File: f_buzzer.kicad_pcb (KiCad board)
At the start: 2 copper layers, 71.5 x 44 mm, 10 parts, among them U1 SN74123N

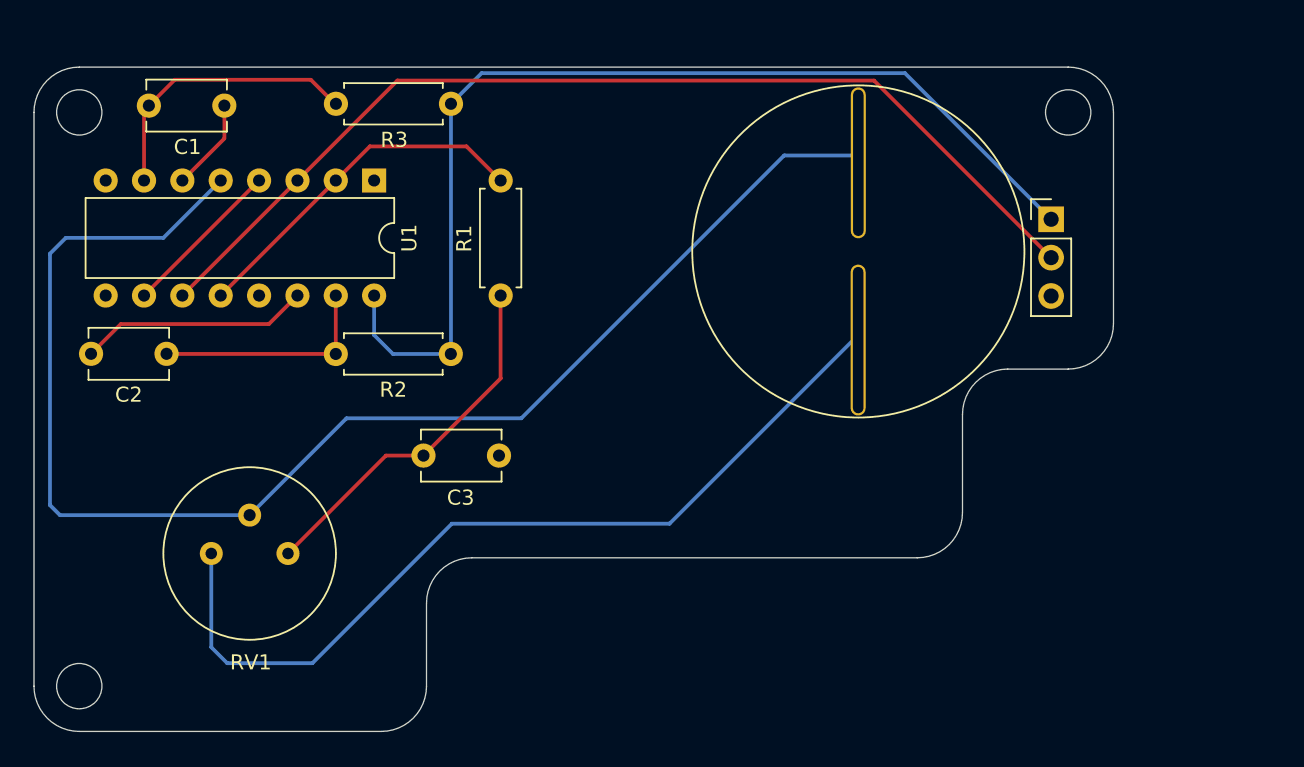
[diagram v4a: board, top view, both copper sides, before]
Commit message: Placed the two buzzers for 3D rendering of the board
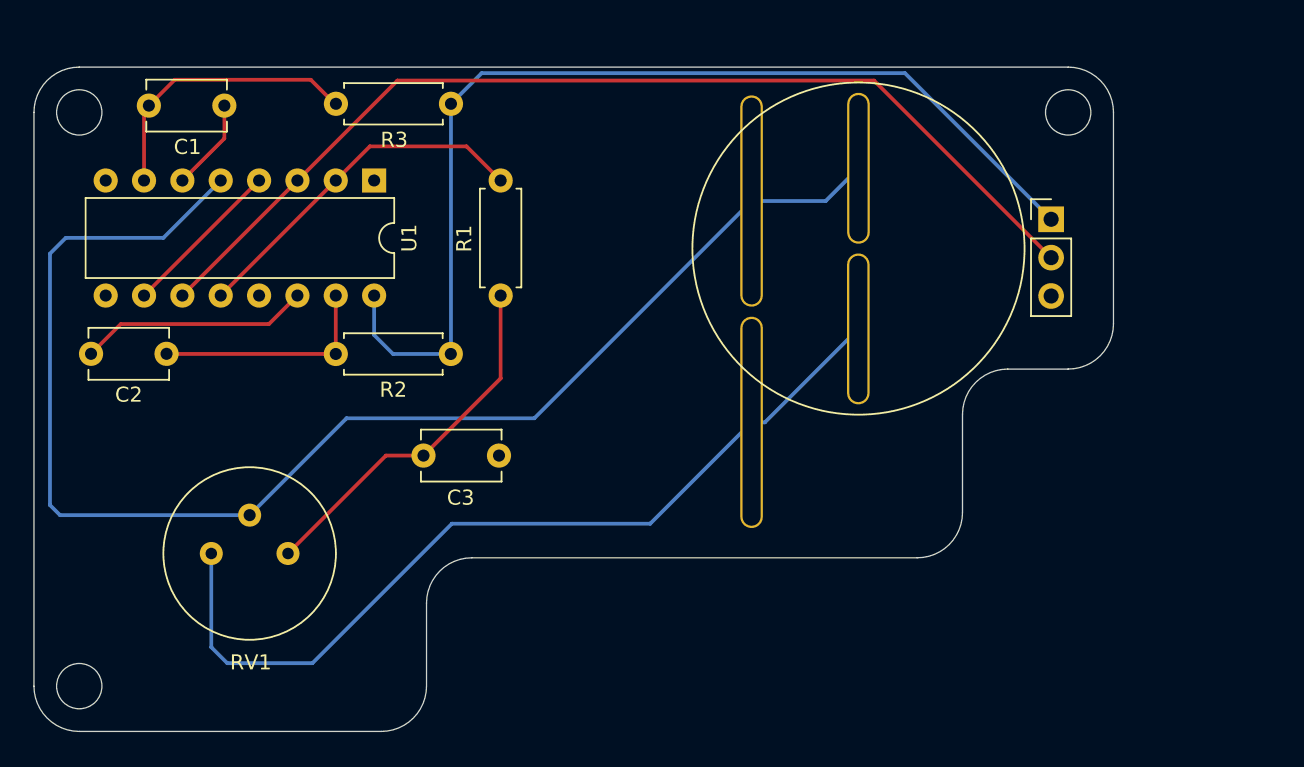
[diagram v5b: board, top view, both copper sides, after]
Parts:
- added BZ1: Buzzer, f_buzzer:buzzer_bottom, B.Cu at (161.7, 92.3)
- moved BZ2 0.19 mm to (168.8, 88.2)
- renumbered BZ1 to BZ2
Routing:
- net Net-(BZ1-Pad1): track 93.8 -> 93.3 mm
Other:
- board text removed: "This is the area where the buzzer could fit on the top of the board."
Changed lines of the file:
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@@
   (general
     (thickness 1.6)
-    (drawings 48)
-    (tracks 51)
+    (drawings 44)
+    (tracks 54)
     (zones 0)
-    (modules 10)
+    (modules 11)
     (nets 14)
   )
@@
     (36 B.SilkS user)
     (37 F.SilkS user)
-    (38 B.Mask user)
-    (39 F.Mask user)
-    (40 Dwgs.User user)
-    (41 Cmts.User user)
+    (38 B.Mask user hide)
+    (39 F.Mask user hide)
+    (40 Dwgs.User user hide)
+    (41 Cmts.User user hide)
     (42 Eco1.User user hide)
     (43 Eco2.User user hide)
@@
     (47 F.CrtYd user hide)
     (48 B.Fab user hide)
-    (49 F.Fab user)
+    (49 F.Fab user hide)
   )
   (setup
@@
     (add_net VCC)
   )
+  (module f_buzzer:buzzer_bottom (layer B.Cu)
+    (at 161.74 92.35 180)
+    (fp_text reference BZ1 (at -0.02 15.2) (layer B.SilkS) hide
+      (effects (font (size 1 1) (thickness 0.15)) (justify mirror))
+    )
+    (fp_text value Buzzer (at -0.09 -15.54) (layer B.Fab)
+      (effects (font (size 1 1) (thickness 0.15)) (justify mirror))
+    )
+    (fp_circle (center 0 0) (end 14.884743 0) (layer B.Fab) (width 0.12))
+    (fp_circle (center 0 0) (end 15 0) (layer B.SilkS) (width 0.12))
+    (pad 2 thru_hole oval (at 0 -7.33 180) (size 1.5 14) (drill oval 1.2 13.7) (layers *.Cu *.Mask)
+      (net 1 "Net-(BZ1-Pad2)"))
+    (pad 1 thru_hole oval (at 0 7.33 180) (size 1.5 14) (drill oval 1.2 13.7) (layers *.Cu *.Mask)
+      (net 2 "Net-(BZ1-Pad1)"))
+    (model f_buzzer.pretty/CUI_DEVICES_CPT-3075-90T.step
+      (offset (xyz 0 0 7.5))
+      (scale (xyz 1 1 1))
+      (rotate (xyz -90 0 -90))
+    )
+  )
   (module f_buzzer:buzzer_front (layer F.Cu)
-    (at 168.81 88.36)
-    (fp_text reference BZ1 (at -0.02 -12.32) (layer F.SilkS) hide
+    (at 168.82 88.17)
+    (fp_text reference BZ2 (at -0.02 -12.32) (layer F.SilkS) hide
       (effects (font (size 1 1) (thickness 0.15)))
     )
@@
       (effects (font (size 1 1) (thickness 0.15)))
     )
-    (fp_circle (center 0 0) (end 8.59 6.68) (layer F.Fab) (width 0.12))
+    (fp_circle (center 0 0) (end 10.881659 0) (layer F.Fab) (width 0.12))
     (fp_circle (center 0 0) (end 11 0) (layer F.SilkS) (width 0.12))
-    (pad 1 thru_hole oval (at 0 -5.87) (size 1 10) (drill oval 0.7 9.7) (layers *.Cu *.Mask)
+    (pad 2 thru_hole oval (at -0.01 5.32) (size 1.5 10) (drill oval 1.2 9.7) (layers *.Cu *.Mask)
+      (net 1 "Net-(BZ1-Pad2)"))
+    (pad 1 thru_hole oval (at 0 -5.32) (size 1.5 10) (drill oval 1.2 9.7) (layers *.Cu *.Mask)
       (net 2 "Net-(BZ1-Pad1)"))
-    (pad 2 thru_hole oval (at -0.01 5.87) (size 1 10) (drill oval 0.7 9.7) (layers *.Cu *.Mask)
-      (net 1 "Net-(BZ1-Pad2)"))
+    (model f_buzzer.pretty/CUI_DEVICES_CPT-2207-84T.step
+      (offset (xyz 0 0 7.5))
+      (scale (xyz 1 1 1))
+      (rotate (xyz -90 0 90))
+    )
   )
   (module Package_DIP:DIP-16_W7.62mm (layer F.Cu)
@@
   (gr_line (start 118.75 76.15) (end 118.75 82) (layer Dwgs.User) (width 0.12))
   (gr_circle (center 179.05 79.2) (end 181.05 79.2) (layer Dwgs.User) (width 0.12))
-  (gr_text "This is the area where the buzzer could fit on the top of the board." (at 207.06 110.52) (layer Cmts.User)
-    (effects (font (size 1 1) (thickness 0.15)))
-  )
-  (gr_line (start 177.82 95.34) (end 178.34 95.37) (layer Cmts.User) (width 0.12))
-  (gr_line (start 177.82 95.34) (end 177.92 95.84) (layer Cmts.User) (width 0.12))
-  (gr_line (start 177.82 95.35) (end 191.65 109.08) (layer Cmts.User) (width 0.12))
   (gr_text "No components should be placed inside the cercle.\nThis where the IBM 4704 series keyboard feet attaches to the back case." (at 120.87 125.39) (layer Cmts.User)
     (effects (font (size 1 1) (thickness 0.15)))
@@
   (gr_line (start 182.71 76.15) (end 117.21 76.15) (layer Edge.Cuts) (width 0.05))
   (gr_line (start 114.21 117.15) (end 114.21 79.15) (layer Edge.Cuts) (width 0.05))
+  (segment (start 125.955 114.575) (end 125.955 108.365) (width 0.25) (layer B.Cu) (net 1))
+  (segment (start 132.65 115.63) (end 127.01 115.63) (width 0.25) (layer B.Cu) (net 1))
+  (segment (start 141.89 106.39) (end 132.65 115.63) (width 0.25) (layer B.Cu) (net 1))
+  (segment (start 155.03 106.39) (end 141.89 106.39) (width 0.25) (layer B.Cu) (net 1))
   (segment (start 127.01 115.63) (end 125.955 114.575) (width 0.25) (layer B.Cu) (net 1))
-  (segment (start 132.65 115.63) (end 127.01 115.63) (width 0.25) (layer B.Cu) (net 1))
-  (segment (start 125.955 114.575) (end 125.955 108.365) (width 0.25) (layer B.Cu) (net 1))
-  (segment (start 156.31 106.39) (end 141.89 106.39) (width 0.25) (layer B.Cu) (net 1))
-  (segment (start 141.89 106.39) (end 132.65 115.63) (width 0.25) (layer B.Cu) (net 1))
-  (segment (start 168.96 93.74) (end 156.31 106.39) (width 0.25) (layer B.Cu) (net 1))
+  (segment (start 161.74 99.68) (end 155.03 106.39) (width 0.25) (layer B.Cu) (net 1))
+  (segment (start 162.62 99.68) (end 168.81 93.49) (width 0.25) (layer B.Cu) (net 1))
+  (segment (start 161.74 99.68) (end 162.62 99.68) (width 0.25) (layer B.Cu) (net 1))
   (segment (start 116.32 87.46) (end 122.78 87.46) (width 0.25) (layer B.Cu) (net 2))
   (segment (start 115.27 88.51) (end 116.32 87.46) (width 0.25) (layer B.Cu) (net 2))
@@
   (segment (start 115.935 105.825) (end 115.27 105.16) (width 0.25) (layer B.Cu) (net 2))
   (segment (start 128.495 105.825) (end 115.935 105.825) (width 0.25) (layer B.Cu) (net 2))
+  (segment (start 147.35 99.41) (end 134.91 99.41) (width 0.25) (layer B.Cu) (net 2))
   (segment (start 134.91 99.41) (end 128.495 105.825) (width 0.25) (layer B.Cu) (net 2))
-  (segment (start 146.49 99.41) (end 134.91 99.41) (width 0.25) (layer B.Cu) (net 2))
-  (segment (start 163.9 82) (end 146.49 99.41) (width 0.25) (layer B.Cu) (net 2))
-  (segment (start 168.97 82) (end 163.9 82) (width 0.25) (layer B.Cu) (net 2))
+  (segment (start 161.74 85.02) (end 147.35 99.41) (width 0.25) (layer B.Cu) (net 2))
+  (segment (start 166.65 85.02) (end 168.82 82.85) (width 0.25) (layer B.Cu) (net 2))
+  (segment (start 161.74 85.02) (end 166.65 85.02) (width 0.25) (layer B.Cu) (net 2))
   (segment (start 121.5 79.02) (end 121.5 83.66) (width 0.25) (layer F.Cu) (net 3))
   (segment (start 121.82 78.7) (end 121.5 79.02) (width 0.25) (layer F.Cu) (net 3))

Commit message: Added fill zones
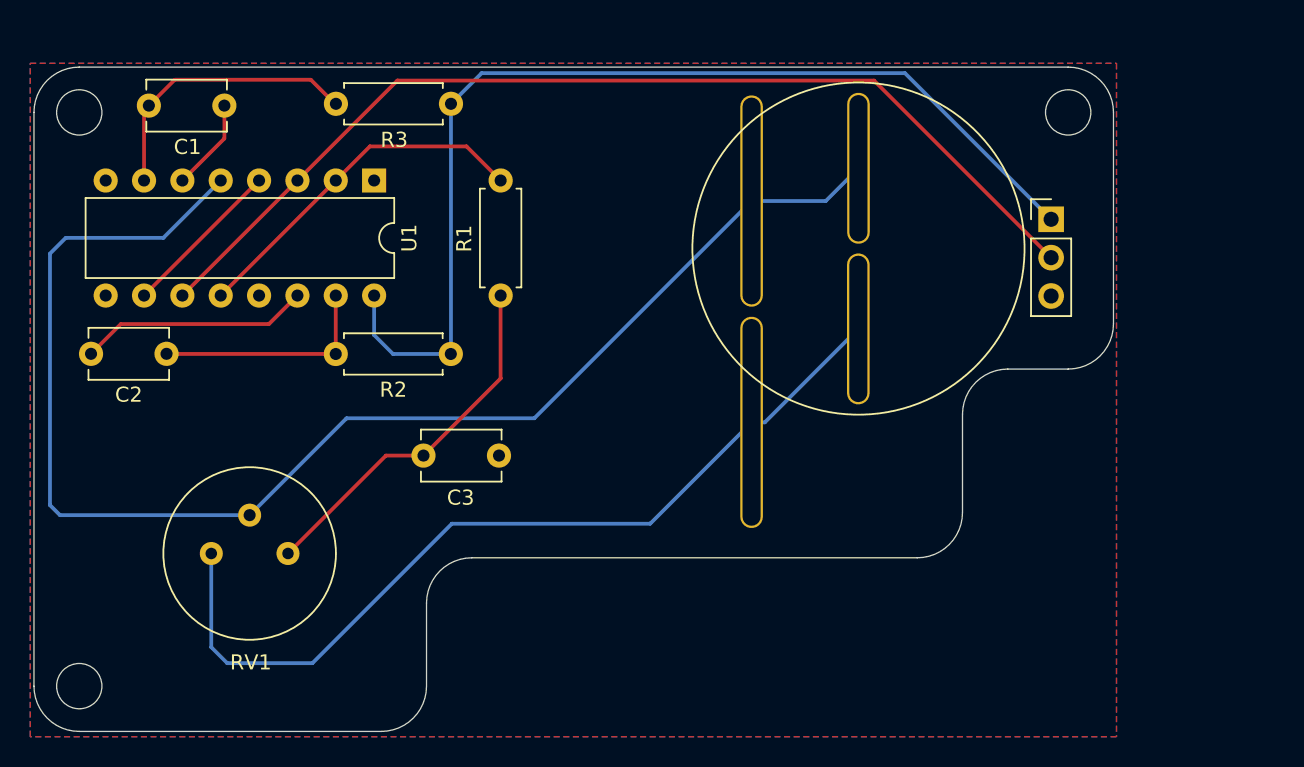
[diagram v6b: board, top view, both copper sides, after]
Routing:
- added copper zone on B.Cu, net GND
- added copper zone on F.Cu, net GND

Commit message: Relocated some components
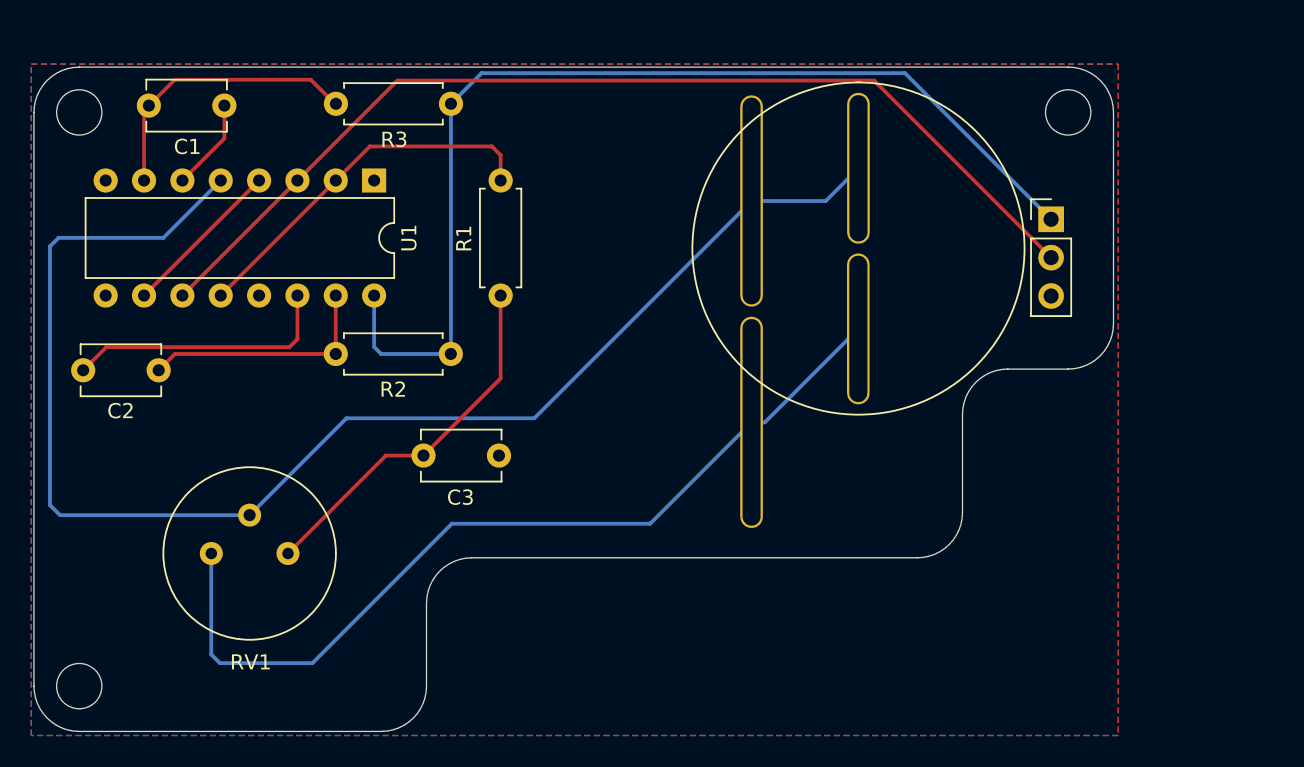
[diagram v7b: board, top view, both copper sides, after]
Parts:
- moved C2 1.21 mm to (117.5, 96.2)
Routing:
- net Net-(C2-Pad1): track 15.3 -> 17.9 mm
- net Net-(R1-Pad1): track 23.6 -> 24.6 mm
- net Net-(C2-Pad2): track 15.1 -> 16.1 mm
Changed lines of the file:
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@@
     (thickness 1.6)
     (drawings 44)
-    (tracks 54)
+    (tracks 56)
     (zones 0)
     (modules 11)
@@
     (38 B.Mask user hide)
     (39 F.Mask user hide)
-    (40 Dwgs.User user hide)
+    (40 Dwgs.User user)
     (41 Cmts.User user hide)
     (42 Eco1.User user hide)
@@
   )
   (module Capacitor_THT:C_Disc_D5.1mm_W3.2mm_P5.00mm (layer F.Cu)
-    (at 117.99 95.14)
+    (at 117.47 96.23)
     (descr "C, Disc series, Radial, pin pitch=5.00mm, , diameter*width=5.1*3.2mm^2, Capacitor, http://www.vishay.com/docs/45233/krseries.pdf")
     (tags "C Disc series Radial pin pitch 5.00mm  diameter 5.1mm width 3.2mm Capacitor")
@@
   (gr_line (start 182.71 76.15) (end 117.21 76.15) (layer Edge.Cuts) (width 0.05))
   (gr_line (start 114.21 117.15) (end 114.21 79.15) (layer Edge.Cuts) (width 0.05))
-  (segment (start 125.955 114.575) (end 125.955 108.365) (width 0.25) (layer B.Cu) (net 1))
-  (segment (start 132.65 115.63) (end 127.01 115.63) (width 0.25) (layer B.Cu) (net 1))
+  (segment (start 162.62 99.68) (end 168.81 93.49) (width 0.25) (layer B.Cu) (net 1))
+  (segment (start 161.74 99.68) (end 162.62 99.68) (width 0.25) (layer B.Cu) (net 1))
+  (segment (start 125.955 115.055) (end 125.955 108.365) (width 0.25) (layer B.Cu) (net 1))
+  (segment (start 126.53 115.63) (end 125.955 115.055) (width 0.25) (layer B.Cu) (net 1))
+  (segment (start 132.65 115.63) (end 126.53 115.63) (width 0.25) (layer B.Cu) (net 1))
   (segment (start 141.89 106.39) (end 132.65 115.63) (width 0.25) (layer B.Cu) (net 1))
   (segment (start 155.03 106.39) (end 141.89 106.39) (width 0.25) (layer B.Cu) (net 1))
-  (segment (start 127.01 115.63) (end 125.955 114.575) (width 0.25) (layer B.Cu) (net 1))
   (segment (start 161.74 99.68) (end 155.03 106.39) (width 0.25) (layer B.Cu) (net 1))
-  (segment (start 162.62 99.68) (end 168.81 93.49) (width 0.25) (layer B.Cu) (net 1))
-  (segment (start 161.74 99.68) (end 162.62 99.68) (width 0.25) (layer B.Cu) (net 1))
-  (segment (start 116.32 87.46) (end 122.78 87.46) (width 0.25) (layer B.Cu) (net 2))
-  (segment (start 115.27 88.51) (end 116.32 87.46) (width 0.25) (layer B.Cu) (net 2))
-  (segment (start 115.27 105.16) (end 115.27 88.51) (width 0.25) (layer B.Cu) (net 2))
-  (segment (start 122.78 87.46) (end 126.58 83.66) (width 0.25) (layer B.Cu) (net 2))
-  (segment (start 115.935 105.825) (end 115.27 105.16) (width 0.25) (layer B.Cu) (net 2))
-  (segment (start 128.495 105.825) (end 115.935 105.825) (width 0.25) (layer B.Cu) (net 2))
   (segment (start 147.35 99.41) (end 134.91 99.41) (width 0.25) (layer B.Cu) (net 2))
   (segment (start 134.91 99.41) (end 128.495 105.825) (width 0.25) (layer B.Cu) (net 2))
@@
   (segment (start 166.65 85.02) (end 168.82 82.85) (width 0.25) (layer B.Cu) (net 2))
   (segment (start 161.74 85.02) (end 166.65 85.02) (width 0.25) (layer B.Cu) (net 2))
+  (segment (start 122.78 87.46) (end 126.58 83.66) (width 0.25) (layer B.Cu) (net 2))
+  (segment (start 115.84 87.46) (end 122.78 87.46) (width 0.25) (layer B.Cu) (net 2))
+  (segment (start 115.27 105.16) (end 115.27 88.03) (width 0.25) (layer B.Cu) (net 2))
+  (segment (start 115.935 105.825) (end 115.27 105.16) (width 0.25) (layer B.Cu) (net 2))
+  (segment (start 115.27 88.03) (end 115.84 87.46) (width 0.25) (layer B.Cu) (net 2))
+  (segment (start 128.495 105.825) (end 115.935 105.825) (width 0.25) (layer B.Cu) (net 2))
   (segment (start 121.5 79.02) (end 121.5 83.66) (width 0.25) (layer F.Cu) (net 3))
   (segment (start 121.82 78.7) (end 121.5 79.02) (width 0.25) (layer F.Cu) (net 3))
@@
   (segment (start 134.2 91.28) (end 134.2 95.15) (width 0.25) (layer F.Cu) (net 5))
   (segment (start 134.19 95.14) (end 134.2 95.15) (width 0.25) (layer F.Cu) (net 5))
-  (segment (start 123 95.15) (end 122.99 95.14) (width 0.25) (layer F.Cu) (net 5))
-  (segment (start 134.2 95.15) (end 123 95.15) (width 0.25) (layer F.Cu) (net 5))
-  (segment (start 119.96 93.17) (end 117.96 95.17) (width 0.25) (layer F.Cu) (net 6))
-  (segment (start 129.77 93.17) (end 119.96 93.17) (width 0.25) (layer F.Cu) (net 6))
-  (segment (start 131.66 91.28) (end 129.77 93.17) (width 0.25) (layer F.Cu) (net 6))
+  (segment (start 123.55 95.15) (end 122.47 96.23) (width 0.25) (layer F.Cu) (net 5))
+  (segment (start 134.2 95.15) (end 123.55 95.15) (width 0.25) (layer F.Cu) (net 5))
+  (segment (start 119 94.7) (end 117.47 96.23) (width 0.25) (layer F.Cu) (net 6))
+  (segment (start 131.66 94.17) (end 131.13 94.7) (width 0.25) (layer F.Cu) (net 6))
+  (segment (start 131.13 94.7) (end 119 94.7) (width 0.25) (layer F.Cu) (net 6))
+  (segment (start 131.66 91.28) (end 131.66 94.17) (width 0.25) (layer F.Cu) (net 6))
   (segment (start 145.12 96.77) (end 140.01 101.88) (width 0.25) (layer F.Cu) (net 8))
   (segment (start 145.12 91.28) (end 145.12 96.77) (width 0.25) (layer F.Cu) (net 8))
@@
   (segment (start 131.035 108.365) (end 137.52 101.88) (width 0.25) (layer F.Cu) (net 8))
   (segment (start 134.2 83.66) (end 126.58 91.28) (width 0.25) (layer F.Cu) (net 9))
-  (segment (start 142.86 81.4) (end 145.12 83.66) (width 0.25) (layer F.Cu) (net 9))
-  (segment (start 136.46 81.4) (end 142.86 81.4) (width 0.25) (layer F.Cu) (net 9))
+  (segment (start 145.12 81.98) (end 145.12 83.66) (width 0.25) (layer F.Cu) (net 9))
+  (segment (start 144.54 81.4) (end 145.12 81.98) (width 0.25) (layer F.Cu) (net 9))
+  (segment (start 136.46 81.4) (end 144.54 81.4) (width 0.25) (layer F.Cu) (net 9))
   (segment (start 134.2 83.66) (end 136.46 81.4) (width 0.25) (layer F.Cu) (net 9))
   (segment (start 141.83 95.14) (end 141.82 95.15) (width 0.25) (layer B.Cu) (net 10))
   (segment (start 141.83 78.58) (end 141.83 95.14) (width 0.25) (layer B.Cu) (net 10))
-  (segment (start 137.99 95.15) (end 141.82 95.15) (width 0.25) (layer B.Cu) (net 10))
-  (segment (start 136.74 93.9) (end 137.99 95.15) (width 0.25) (layer B.Cu) (net 10))
-  (segment (start 136.74 91.28) (end 136.74 93.9) (width 0.25) (layer B.Cu) (net 10))
   (segment (start 143.86 76.55) (end 141.83 78.58) (width 0.25) (layer B.Cu) (net 10))
   (segment (start 171.9 76.55) (end 143.86 76.55) (width 0.25) (layer B.Cu) (net 10))
   (segment (start 181.58 86.23) (end 171.9 76.55) (width 0.25) (layer B.Cu) (net 10))
+  (segment (start 137.2 95.15) (end 141.82 95.15) (width 0.25) (layer B.Cu) (net 10))
+  (segment (start 136.74 94.69) (end 137.2 95.15) (width 0.25) (layer B.Cu) (net 10))
+  (segment (start 136.74 91.28) (end 136.74 94.69) (width 0.25) (layer B.Cu) (net 10))
   (segment (start 131.66 83.66) (end 124.04 91.28) (width 0.25) (layer F.Cu) (net 12))
+  (segment (start 169.85 77.04) (end 138.28 77.04) (width 0.25) (layer F.Cu) (net 12))
   (segment (start 138.28 77.04) (end 131.66 83.66) (width 0.25) (layer F.Cu) (net 12))
-  (segment (start 169.85 77.04) (end 138.28 77.04) (width 0.25) (layer F.Cu) (net 12))
   (segment (start 181.58 88.77) (end 169.85 77.04) (width 0.25) (layer F.Cu) (net 12))
   (segment (start 129.12 83.66) (end 121.5 91.28) (width 0.25) (layer F.Cu) (net 13))
@@
     (polygon
       (pts
-        (xy 185.91 120.5) (xy 113.96 120.5) (xy 113.96 75.9) (xy 185.91 75.9)
+        (xy 186.03 120.42) (xy 114.03 120.42) (xy 114.03 75.95) (xy 186.03 75.95)
       )
     )
@@
     (polygon
       (pts
-        (xy 185.91 120.5) (xy 113.96 120.5) (xy 113.96 75.9) (xy 185.91 75.9)
+        (xy 186.03 120.42) (xy 114.03 120.42) (xy 114.03 75.95) (xy 186.03 75.95)
       )
     )

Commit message: Added JLCPCB magic string
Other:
- board text added: "JLCJLCJLCJLC"
